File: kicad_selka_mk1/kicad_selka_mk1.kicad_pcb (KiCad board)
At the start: 2 copper layers, 95.2 x 160.3 mm, 76 parts, among them J1 Conn_01x06_Pin, J2 Conn_01x02_Pin, U1 ATtiny861A-S

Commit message: Ahasta
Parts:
- D1, D10, D11, D12, D13, D14, D15, D16, D17, D18, D19, D2, D20, D21, D22, D23, D24, D25, D26, D27, D28, D29, D3, D30, D31, D32, D33, D34, D35, D36, D37, D38, D39, D4, D40, D41, D42, D43, D44, D45, D46, D47, D48, D49, D5, D50, D51, D52, D53, D54, D55, D56, D57, D58, D59, D6, D60, D61, D62, D63, D64, D7, D8, D9: footprint Library_zani:LED_D5.0mm_1.2_reikamod -> LED_THT:LED_D5.0mm
- J1, J2, R2, R3, U1: moved to B.Cu
- moved R5 88.5 mm to (151.9, 155.7)
- moved R4 82.6 mm to (141.5, 179.6), turned to -90 degrees
- moved R3 72.4 mm to (134.4, 166.9)
- moved U1 57.3 mm to (119.6, 125.9), turned to 0 degrees
- moved R1 46.2 mm to (125.0, 112.8)
- moved R2 46.0 mm to (125.7, 134.1)
- moved J2 45.4 mm to (122.7, 117.6), turned to -90 degrees
- moved R6 41.5 mm to (119.6, 137.9)
- moved D26 33.7 mm to (111.5, 238.3)
- moved C1 33.5 mm to (105.4, 124.8), turned to 90 degrees
- moved J1 29.1 mm to (110.5, 126.4), turned to 0 degrees
- moved R8 28.5 mm to (116.6, 111.8)
- moved D27 28.3 mm to (117.9, 228.1)
- moved D28 26.5 mm to (121.9, 221.0)
- moved D29 24.0 mm to (126.2, 213.4)
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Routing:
- net Net-(D16-K): track 0.00 -> 210.2 mm, vias 0 -> 2
- net Net-(D1-K): track 0.00 -> 206.5 mm, vias 0 -> 3
- net Net-(D10-K): track 0.00 -> 204.3 mm, vias 0 -> 4
- net Net-(D14-K): track 0.00 -> 160.0 mm, vias 0 -> 4
- net Net-(D15-K): track 0.00 -> 159.3 mm, vias 0 -> 5
- net Net-(D11-K): track 0.00 -> 99.2 mm, vias 0 -> 2
- net Net-(D13-K): track 0.00 -> 98.7 mm, vias 0 -> 4
- net Net-(D25-A): track 0.00 -> 75.5 mm
- net Net-(D33-A): track 0.00 -> 73.4 mm
- net Net-(D17-A): track 0.00 -> 68.3 mm
- net Net-(D49-A): track 0.00 -> 64.2 mm
- net Net-(D12-K): track 0.00 -> 61.1 mm, vias 0 -> 2
- net Net-(D41-A): track 0.00 -> 59.3 mm
- net Net-(D10-A): track 0.00 -> 56.0 mm
- net Net-(D57-A): track 0.00 -> 55.6 mm
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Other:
- board size 95.2 x 160.3 mm -> 92.7 x 200.4 mm

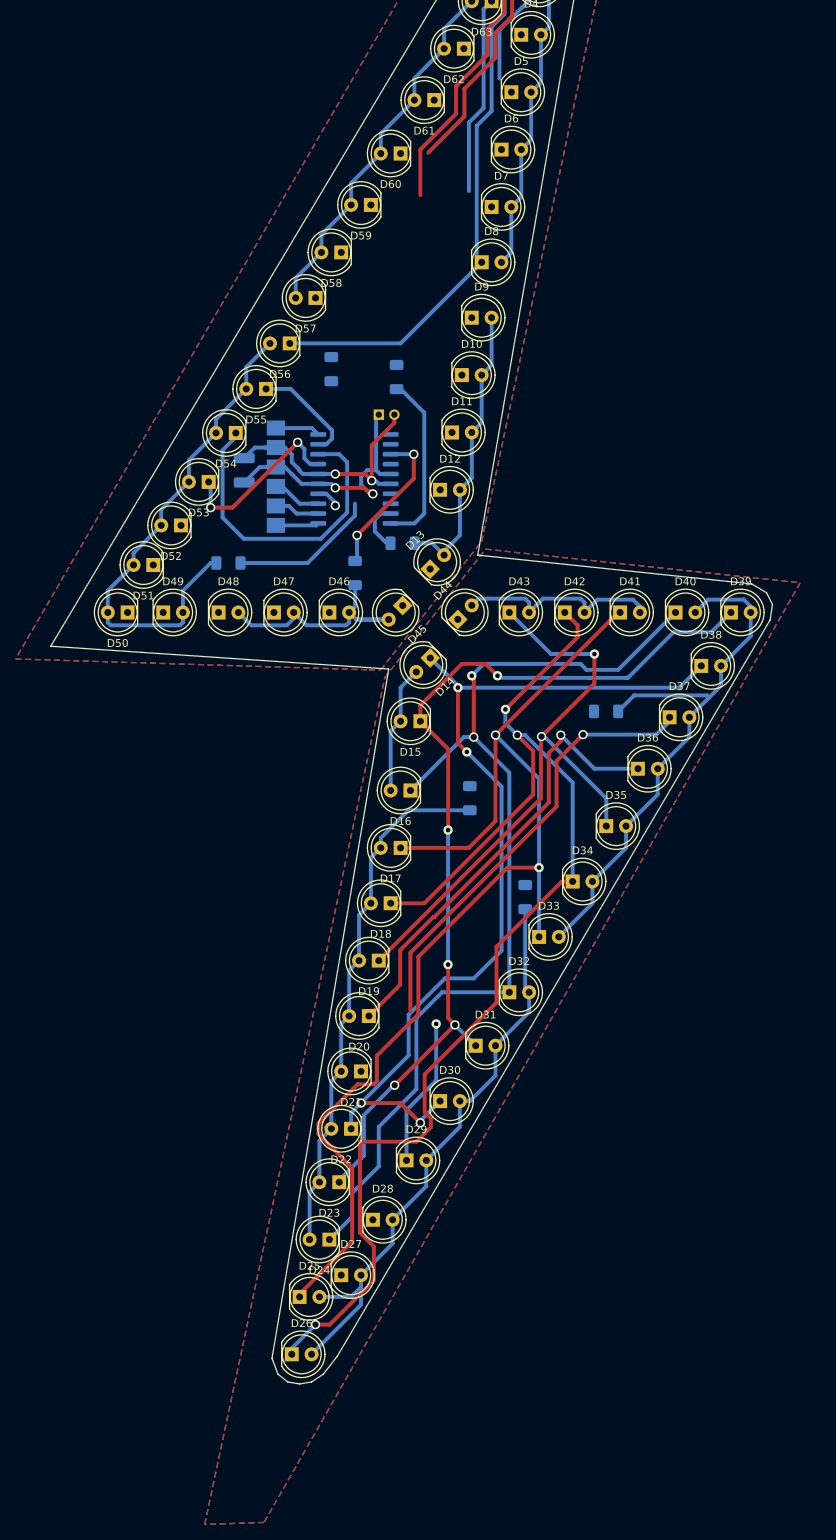
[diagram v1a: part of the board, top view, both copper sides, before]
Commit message: Selkäsalaman skemaan lisätty jumperit
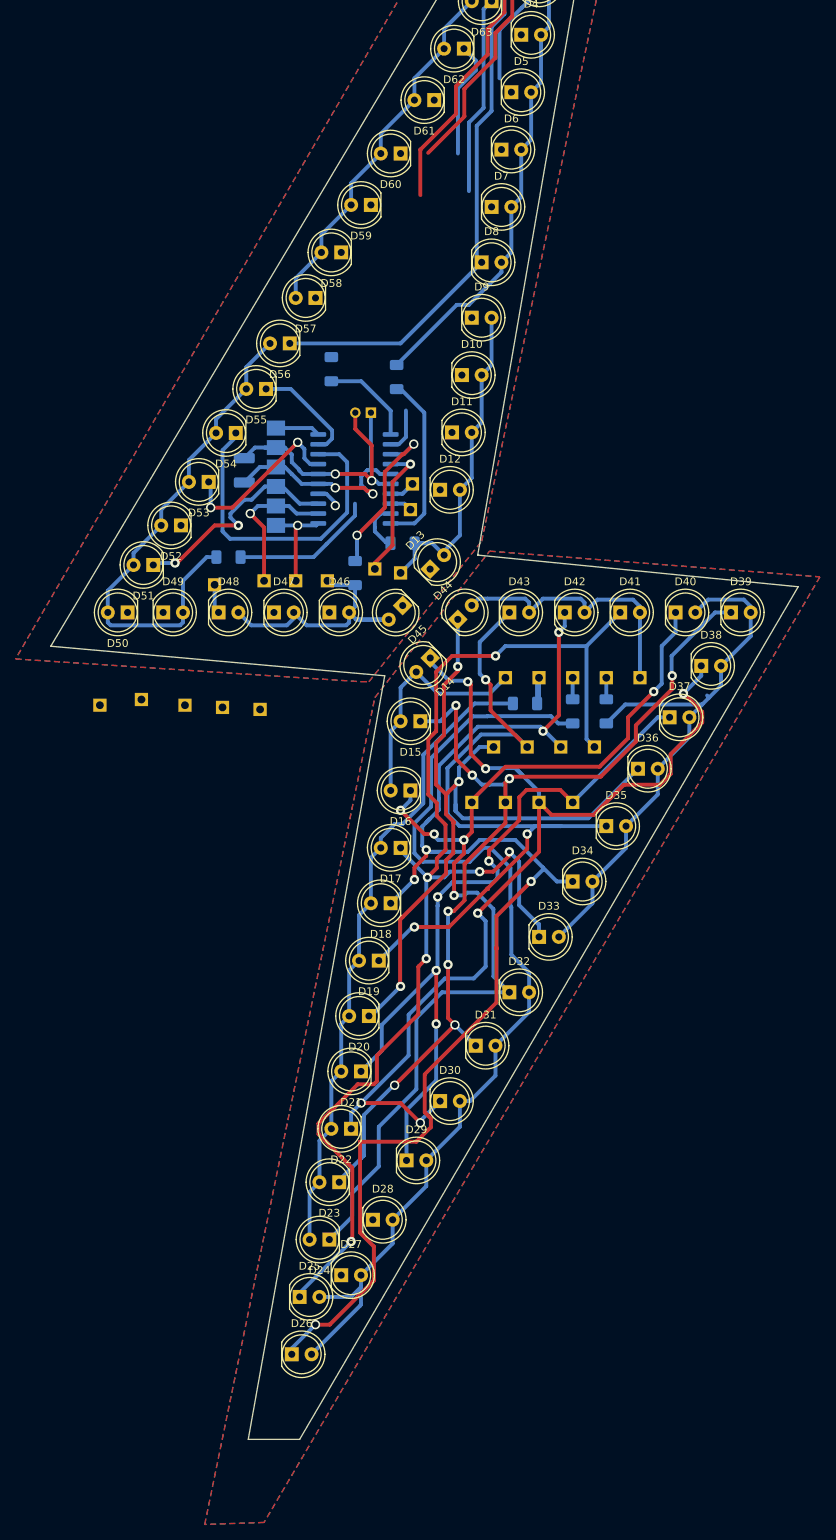
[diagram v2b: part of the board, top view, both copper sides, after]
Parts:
- added J10: Conn_01x01_Pin, Connector_PinSocket_2.54mm:PinSocket_1x01_P2.54mm_Vertical, B.Cu at (151.9, 151.4)
- added J11: Conn_01x01_Pin, Connector_PinSocket_2.54mm:PinSocket_1x01_P2.54mm_Vertical, B.Cu at (116.1, 138.9)
- added J12: Conn_01x01_Pin, Connector_PinSocket_2.54mm:PinSocket_1x01_P2.54mm_Vertical, B.Cu at (156.2, 151.4)
- added J13: Conn_01x01_Pin, Connector_PinSocket_2.54mm:PinSocket_1x01_P2.54mm_Vertical, B.Cu at (112.0, 138.9)
- added J14: Conn_01x01_Pin, Connector_PinSocket_2.54mm:PinSocket_1x01_P2.54mm_Vertical, B.Cu at (150.4, 160.3)
- added J15: Conn_01x01_Pin, Connector_PinSocket_2.54mm:PinSocket_1x01_P2.54mm_Vertical, B.Cu at (108.0, 138.9)
- added J16: Conn_01x01_Pin, Connector_PinSocket_2.54mm:PinSocket_1x01_P2.54mm_Vertical, B.Cu at (146.1, 160.3)
- added J17: Conn_01x01_Pin, Connector_PinSocket_2.54mm:PinSocket_1x01_P2.54mm_Vertical, B.Cu at (107.4, 155.4)
- added J18: Conn_01x01_Pin, Connector_PinSocket_2.54mm:PinSocket_1x01_P2.54mm_Vertical, B.Cu at (141.7, 160.3)
- added J19: Conn_01x01_Pin, Connector_PinSocket_2.54mm:PinSocket_1x01_P2.54mm_Vertical, B.Cu at (102.6, 155.2)
- added J20: Conn_01x01_Pin, Connector_PinSocket_2.54mm:PinSocket_1x01_P2.54mm_Vertical, B.Cu at (137.4, 160.3)
- added J21: Conn_01x01_Pin, Connector_PinSocket_2.54mm:PinSocket_1x01_P2.54mm_Vertical, B.Cu at (97.8, 154.9)
- added J22: Conn_01x01_Pin, Connector_PinSocket_2.54mm:PinSocket_1x01_P2.54mm_Vertical, B.Cu at (147.6, 167.4)
- added J23: Conn_01x01_Pin, Connector_PinSocket_2.54mm:PinSocket_1x01_P2.54mm_Vertical, B.Cu at (92.2, 154.2)
- added J24: Conn_01x01_Pin, Connector_PinSocket_2.54mm:PinSocket_1x01_P2.54mm_Vertical, B.Cu at (143.3, 167.4)
- added J25: Conn_01x01_Pin, Connector_PinSocket_2.54mm:PinSocket_1x01_P2.54mm_Vertical, B.Cu at (86.9, 154.9)
- added J26: Conn_01x01_Pin, Connector_PinSocket_2.54mm:PinSocket_1x01_P2.54mm_Vertical, B.Cu at (138.9, 167.4)
- added J27: Conn_01x01_Pin, Connector_PinSocket_2.54mm:PinSocket_1x01_P2.54mm_Vertical, B.Cu at (101.6, 139.4)
- added J28: Conn_01x01_Pin, Connector_PinSocket_2.54mm:PinSocket_1x01_P2.54mm_Vertical, B.Cu at (134.6, 167.4)
- added J3: Conn_01x01_Pin, Connector_PinSocket_2.54mm:PinSocket_1x01_P2.54mm_Vertical, B.Cu at (125.5, 137.9)
- added J4: Conn_01x01_Pin, Connector_PinSocket_2.54mm:PinSocket_1x01_P2.54mm_Vertical, B.Cu at (138.9, 151.4)
- added J5: Conn_01x01_Pin, Connector_PinSocket_2.54mm:PinSocket_1x01_P2.54mm_Vertical, B.Cu at (126.7, 129.8)
- added J6: Conn_01x01_Pin, Connector_PinSocket_2.54mm:PinSocket_1x01_P2.54mm_Vertical, B.Cu at (143.3, 151.4)
- added J7: Conn_01x01_Pin, Connector_PinSocket_2.54mm:PinSocket_1x01_P2.54mm_Vertical, B.Cu at (127.0, 126.5)
- added J8: Conn_01x01_Pin, Connector_PinSocket_2.54mm:PinSocket_1x01_P2.54mm_Vertical, B.Cu at (147.6, 151.4)
- added J9: Conn_01x01_Pin, Connector_PinSocket_2.54mm:PinSocket_1x01_P2.54mm_Vertical, B.Cu at (122.2, 137.4)
- moved R4 24.6 mm to (147.6, 155.7)
- moved R3 14.1 mm to (141.5, 154.7), turned to 180 degrees
- moved J2 1.05 mm to (121.7, 117.3), turned to 90 degrees
- moved R7 0.76 mm to (103.4, 135.9)
- turned R5 to -90 degrees
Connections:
- D14 pad 2: Net-(D10-A) -> Net-(D14-A)
- D15 pad 2: Net-(D10-A) -> Net-(D14-A)
- D16 pad 2: Net-(D10-A) -> Net-(D14-A)
- D17 pad 1: Net-(D1-K) -> Net-(D17-K)
- D18 pad 1: Net-(D10-K) -> Net-(D18-K)
- D19 pad 1: Net-(D11-K) -> Net-(D19-K)
- D20 pad 1: Net-(D12-K) -> Net-(D20-K)
- D21 pad 1: Net-(D13-K) -> Net-(D21-K)
- D25 pad 1: Net-(D1-K) -> Net-(D17-K)
- D26 pad 1: Net-(D10-K) -> Net-(D18-K)
- D27 pad 1: Net-(D11-K) -> Net-(D19-K)
- D28 pad 1: Net-(D12-K) -> Net-(D20-K)
- D29 pad 1: Net-(D13-K) -> Net-(D21-K)
- D33 pad 1: Net-(D1-K) -> Net-(D17-K)
- D34 pad 1: Net-(D10-K) -> Net-(D18-K)
- D35 pad 1: Net-(D11-K) -> Net-(D19-K)
- D36 pad 1: Net-(D12-K) -> Net-(D20-K)
- D37 pad 1: Net-(D13-K) -> Net-(D21-K)
- D41 pad 1: Net-(D1-K) -> Net-(D17-K)
- D42 pad 1: Net-(D10-K) -> Net-(D18-K)
- D43 pad 1: Net-(D11-K) -> Net-(D19-K)
- D44 pad 1: Net-(D12-K) -> Net-(D20-K)
- D45 pad 2: Net-(D41-A) -> Net-(D45-A)
- D46 pad 1: Net-(D14-K) -> Net-(D46-K)
- D46 pad 2: Net-(D41-A) -> Net-(D45-A)
- D47 pad 1: Net-(D15-K) -> Net-(D47-K)
- D47 pad 2: Net-(D41-A) -> Net-(D45-A)
- D48 pad 1: Net-(D16-K) -> Net-(D48-K)
- D48 pad 2: Net-(D41-A) -> Net-(D45-A)
- D54 pad 1: Net-(D14-K) -> Net-(D46-K)
- D55 pad 1: Net-(D15-K) -> Net-(D47-K)
- D56 pad 1: Net-(D16-K) -> Net-(D48-K)
- D57 pad 2: Net-(D57-A) -> Net-(D20-K)
- D58 pad 2: Net-(D57-A) -> Net-(D20-K)
- D59 pad 2: Net-(D57-A) -> Net-(D20-K)
- D6 pad 1: Net-(D14-K) -> Net-(D46-K)
- D60 pad 2: Net-(D57-A) -> Net-(D20-K)
- D61 pad 2: Net-(D57-A) -> Net-(D20-K)
- D62 pad 1: Net-(D14-K) -> Net-(D46-K)
- D62 pad 2: Net-(D57-A) -> Net-(D20-K)
- D63 pad 1: Net-(D15-K) -> Net-(D47-K)
- D63 pad 2: Net-(D57-A) -> Net-(D20-K)
- D64 pad 1: Net-(D16-K) -> Net-(D48-K)
- D64 pad 2: Net-(D57-A) -> Net-(D20-K)
- D7 pad 1: Net-(D15-K) -> Net-(D47-K)
- D8 pad 1: Net-(D16-K) -> Net-(D48-K)
- J1 pad 6: Net-(D16-K) -> Net-(D48-K)
- R3 pad 1: Net-(U1-PA2) -> Net-(J6-Pin_1)
- R4 pad 1: Net-(U1-AREF/PA3) -> Net-(J8-Pin_1)
- R5 pad 1: Net-(U1-PA4) -> Net-(J10-Pin_1)
- R6 pad 2: Net-(D41-A) -> Net-(D45-A)
- R8 pad 2: Net-(D57-A) -> Net-(D20-K)
- U1 pad 10: Net-(D16-K) -> Net-(D48-K)
- U1 pad 14: Net-(U1-PA4) -> Net-(J9-Pin_1)
- U1 pad 17: Net-(U1-AREF/PA3) -> Net-(J7-Pin_1)
- U1 pad 18: Net-(U1-PA2) -> Net-(J5-Pin_1)
- U1 pad 8: Net-(D14-K) -> Net-(D46-K)
- U1 pad 9: Net-(D15-K) -> Net-(D47-K)
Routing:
- net Net-(D18-K): track 0.00 -> 164.8 mm, vias 0 -> 6
- net Net-(D17-K): track 0.00 -> 164.7 mm, vias 0 -> 6
- net Net-(D20-K): track 0.00 -> 154.1 mm, vias 0 -> 3
- net Net-(D10-K): track 204.3 -> 57.7 mm, vias 4 -> 2
- net Net-(D1-K): track 206.5 -> 63.2 mm, vias 3 -> 2
- net Net-(D21-K): track 0.00 -> 98.6 mm, vias 0 -> 4
- net Net-(D19-K): track 0.00 -> 92.9 mm, vias 0 -> 3
- net Net-(D48-K): track 0.00 -> 81.3 mm
- net Net-(D16-K): track 210.2 -> 131.9 mm, vias 2 -> 5
- net Net-(D13-K): track 98.7 -> 22.5 mm, vias 4 -> 2
- net Net-(D12-K): track 61.1 -> 3.04 mm, vias 2 -> 1
- net Net-(D11-K): track 99.2 -> 42.1 mm
- net Net-(D46-K): track 0.00 -> 56.8 mm
- net Net-(D57-A): track 55.6 -> 0.00 mm
- net Net-(D25-A): track 75.5 -> 130.8 mm
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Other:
- board size 92.7 x 200.4 mm -> 96 x 207.5 mm
- board text added: "${REFERENCE}"

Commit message: Selkäsalama 90% done
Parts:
- moved J25 47.0 mm to (113.3, 116.1)
- moved J19 37.1 mm to (127.3, 127.5)
- moved J23 31.5 mm to (105.2, 125.5)
- moved J21 29.7 mm to (122.7, 138.7)
- moved R7 28.1 mm to (115.3, 110.5)
- moved J17 26.3 mm to (105.2, 129.3)
- moved C1 18.0 mm to (120.4, 114.8), turned to 180 degrees
- moved R6 15.7 mm to (103.9, 137.9)
- moved J7 14.0 mm to (115.8, 134.9)
- moved J27 13.2 mm to (114.8, 138.7)
- moved J9 10.7 mm to (111.8, 134.9)
- moved J15 10.7 mm to (118.6, 138.7)
- moved R8 10.0 mm to (126.0, 108.2)
- moved J11 8.89 mm to (107.2, 138.7)
- moved J5 8.52 mm to (119.9, 134.8)
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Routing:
- net Net-(D12-K): track 3.04 -> 105.9 mm, vias 1 -> 6
- net Net-(D10-K): track 57.7 -> 142.3 mm, vias 2 -> 6
- net Net-(D11-K): track 42.1 -> 102.2 mm
- net Net-(D1-K): track 63.2 -> 122.5 mm, vias 2 -> 5
- net Net-(D13-K): track 22.5 -> 66.6 mm, vias 2 -> 3
- net Net-(D47-K): track 39.4 -> 77.1 mm, vias 0 -> 2
- net Net-(D46-K): track 56.8 -> 84.0 mm, vias 0 -> 4
- net Net-(D48-K): track 81.3 -> 106.1 mm, vias 0 -> 1
- net Net-(D20-K): track 154.1 -> 171.4 mm
- net +5V: track 34.6 -> 43.1 mm, vias 2 -> 0
- net Net-(J7-Pin_1): track 3.32 -> 11.5 mm
- net Net-(J5-Pin_1): track 2.86 -> 8.43 mm
- net Net-(U1-PA5): track 23.5 -> 27.4 mm
- net Net-(D45-A): track 35.6 -> 39.3 mm
- net Net-(D10-A): track 43.9 -> 40.6 mm
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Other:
- board size 96 x 207.5 mm -> 89.4 x 199.9 mm
- board text removed: "${REFERENCE}"

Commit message: Selkäsalama 95% done
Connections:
- D57 pad 2: Net-(D20-K) -> Net-(D57-A)
- D58 pad 2: Net-(D20-K) -> Net-(D57-A)
- D59 pad 2: Net-(D20-K) -> Net-(D57-A)
- D60 pad 2: Net-(D20-K) -> Net-(D57-A)
- D61 pad 2: Net-(D20-K) -> Net-(D57-A)
- D62 pad 2: Net-(D20-K) -> Net-(D57-A)
- D63 pad 2: Net-(D20-K) -> Net-(D57-A)
- D64 pad 2: Net-(D20-K) -> Net-(D57-A)
- R8 pad 2: Net-(D20-K) -> Net-(D57-A)
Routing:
- net Net-(D57-A): track 0.00 -> 74.1 mm
- net Net-(D20-K): track 171.4 -> 98.5 mm
- net Net-(D11-K): track 102.2 -> 158.1 mm, vias 2 -> 5
- net Net-(D13-K): track 66.6 -> 104.6 mm, vias 3 -> 5
- net Net-(D48-K): track 106.1 -> 135.9 mm, vias 1 -> 2
- net Net-(D47-K): track 77.1 -> 99.1 mm, vias 2 -> 3
- net Net-(D1-K): track 122.5 -> 137.0 mm
- net Net-(D10-K): track 142.3 -> 146.2 mm
- net Net-(D12-K): track 105.9 -> 102.5 mm
- net Net-(U1-PA5): track 27.4 -> 28.2 mm

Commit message: Selkäsalama redo
1 ledi meni väärälle puolelle -> 31 & 33 lediä :C

Samahan se oli tehdä koko leiska uudelleen parammilla array
ledipaikoilla...
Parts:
- removed the D27 at (117.9, 228.1)
- added D45: LED, LED_THT:LED_D5.0mm, F.Cu at (132.8, 143.9)
- added R9: 110, Resistor_SMD:R_1206_3216Metric_Pad1.30x1.75mm_HandSolder, F.Cu at (95.2, 63.2)
- moved D27 92.4 mm to (118.7, 225.3)
- moved J11 66.7 mm to (42.0, 124.9)
- moved J13 66.7 mm to (45.8, 124.9)
- moved J21 66.7 mm to (57.5, 124.9)
- moved J27 66.7 mm to (49.6, 124.9)
- moved J5 66.7 mm to (54.7, 121.0)
- moved J9 66.7 mm to (46.5, 121.1)
- moved J15 66.7 mm to (53.4, 124.9)
- moved J3 66.7 mm to (58.7, 121.1)
- moved J7 66.7 mm to (50.6, 121.1)
- moved J19 62.9 mm to (68.4, 105.3)
- moved J1 61.2 mm to (57.8, 95.2)
- moved J2 59.3 mm to (65.5, 92.0)
- moved J17 58.9 mm to (48.5, 113.4)
- moved R6 54.5 mm to (68.4, 96.5)
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- renumbered D40 to D27, D45 to D40
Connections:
- D27 pad 1: Net-(D16-K) -> Net-(D19-K)
- D27 pad 2: Net-(D33-A) -> Net-(D25-A)
- D40 pad 1: Net-(D13-K) -> Net-(D16-K)
- D40 pad 2: Net-(D45-A) -> Net-(D33-A)
- D46 pad 2: Net-(D45-A) -> Net-(D46-A)
- D47 pad 2: Net-(D45-A) -> Net-(D46-A)
- D48 pad 2: Net-(D45-A) -> Net-(D46-A)
- J11 pad 1: Net-(D45-A) -> Net-(D46-A)
- R6 pad 2: Net-(D45-A) -> Net-(D46-A)
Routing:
- net Net-(D11-K): track 158.1 -> 0.00 mm, vias 5 -> 0
- net Net-(D10-K): track 146.2 -> 0.00 mm, vias 6 -> 0
- net Net-(D1-K): track 137.0 -> 0.00 mm, vias 5 -> 0
- net Net-(D48-K): track 135.9 -> 0.00 mm, vias 2 -> 0
- net Net-(D13-K): track 104.6 -> 0.00 mm, vias 5 -> 0
- net Net-(D12-K): track 102.5 -> 0.00 mm, vias 6 -> 0
- net Net-(D47-K): track 99.1 -> 0.00 mm, vias 3 -> 0
- net Net-(D46-K): track 84.3 -> 0.00 mm, vias 4 -> 0
- net Net-(D19-K): track 92.9 -> 155.3 mm, vias 3 -> 5
- net +5V: track 43.1 -> 0.00 mm
- net Net-(D45-A): track 39.3 -> 0.00 mm
- net GND: track 33.0 -> 0.00 mm, vias 3 -> 0
- net Net-(D20-K): track 98.5 -> 129.4 mm, vias 3 -> 5
- net Net-(D15-K): track 128.2 -> 156.7 mm, vias 8 -> 6
- net Net-(U1-PA5): track 28.2 -> 0.00 mm, vias 2 -> 0
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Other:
- board size 89.4 x 199.9 mm -> 103.1 x 218.5 mm
- board text added: "Zäni"
